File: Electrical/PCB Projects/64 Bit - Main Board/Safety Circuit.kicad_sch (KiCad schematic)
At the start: 33 parts, among them K1 JS-12N-K, K2 JS-12N-K, K3 JS-12N-K, Q1 2N7002, Q2 XP231P0201TR-G, Q4 2N7002, Q5 2N7002, Q6 XP231P0201TR-G, Q8 2N7002, Q9 2N7002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

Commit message: slight changes
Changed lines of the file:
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@@
 		)
 		(property "Value" "10kohm_0603"
-			(at 113.03 132.334 90)
+			(at 113.284 128.27 90)
 			(effects
 				(font
@@
 		)
 		(property "Value" "10kohm_0603"
-			(at 120.65 132.334 90)
-			(effects
-				(font
+			(at 120.65 128.524 90)
+			(effects
+				(font

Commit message: adding comments after build. Documentation for next revision
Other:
- note added: "P-Channel not suitable try: SQ2389CES-T1_GE3 default gate voltage must be 12V"
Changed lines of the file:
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@@
+		)
+	)
+	(text "P-Channel not suitable try: \nSQ2389CES-T1_GE3\ndefault gate voltage must be 12V"
+		(exclude_from_sim no)
+		(at 38.354 44.45 0)
+		(effects
+			(font
+				(size 1.905 1.905)
+				(thickness 0.381)
+				(bold yes)
+				(color 255 46 77 1)
+			)
+			(justify left)
 		)
 	)

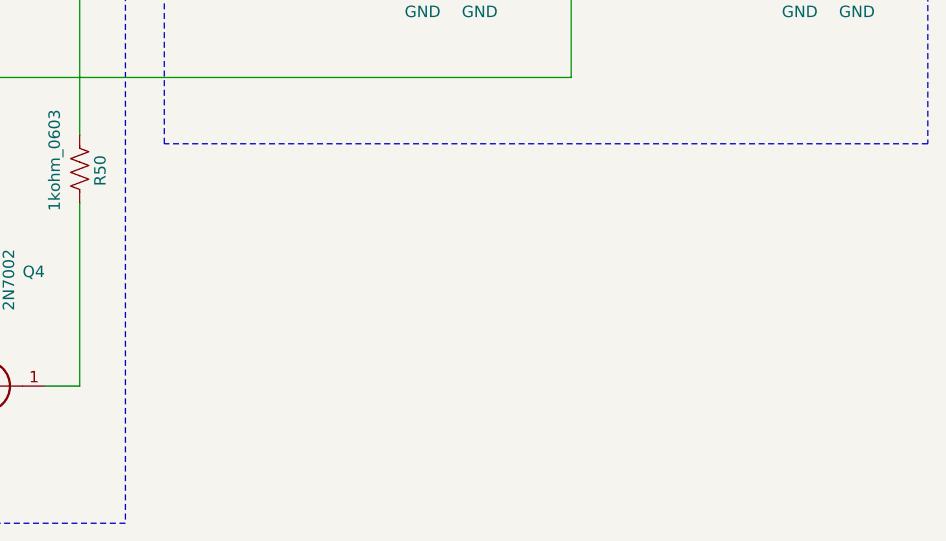
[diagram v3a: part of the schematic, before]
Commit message: mistake found in the safety circuit. The AND gate is mis-designed for mosfets. Two Pchannel mosfets need to be added and the output signal then inverted. These were added via wires to the hardware and the issue is resolved. Adding notes into the schematic
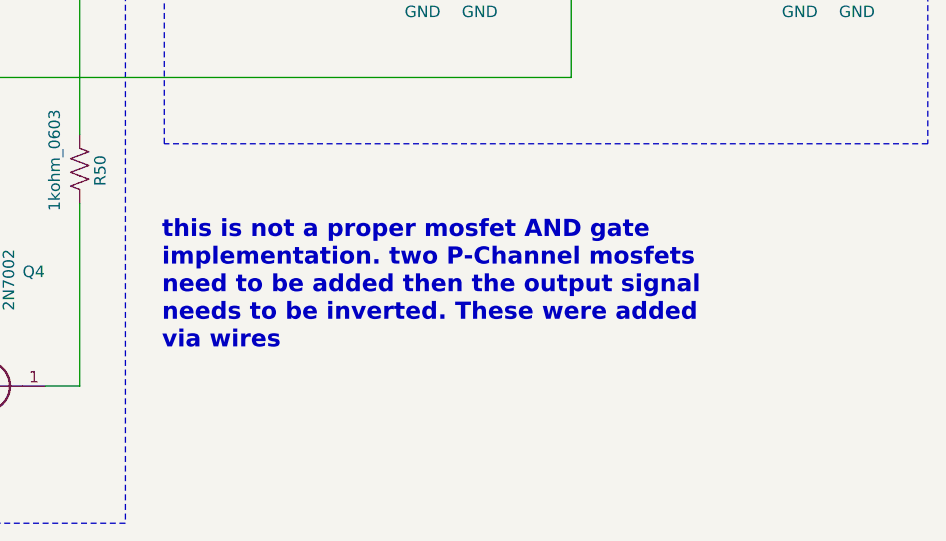
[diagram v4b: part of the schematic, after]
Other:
- note added: "this is not a proper mosfet AND gate implementation. two P-Channel mosfets need to be added then the output signal needs to be inverted. These were added via wires"
